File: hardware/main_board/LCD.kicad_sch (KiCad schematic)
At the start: 2 parts, among them J5 2x5 Socket Pins, U2 HiLetGo_ST7735R

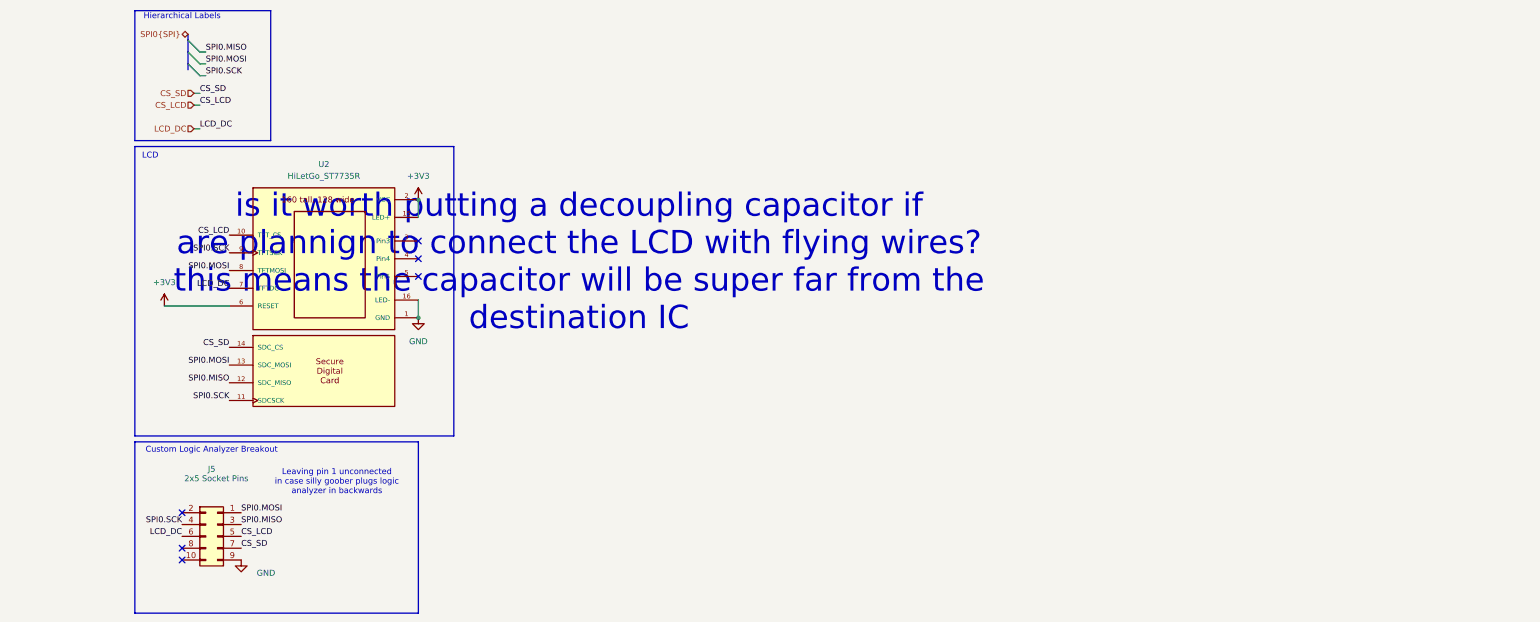
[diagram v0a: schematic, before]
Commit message: main board stuff. removed usbc for power. added level shifter for led logic signal. added lights for mux select signals. finished layout + pass DRC
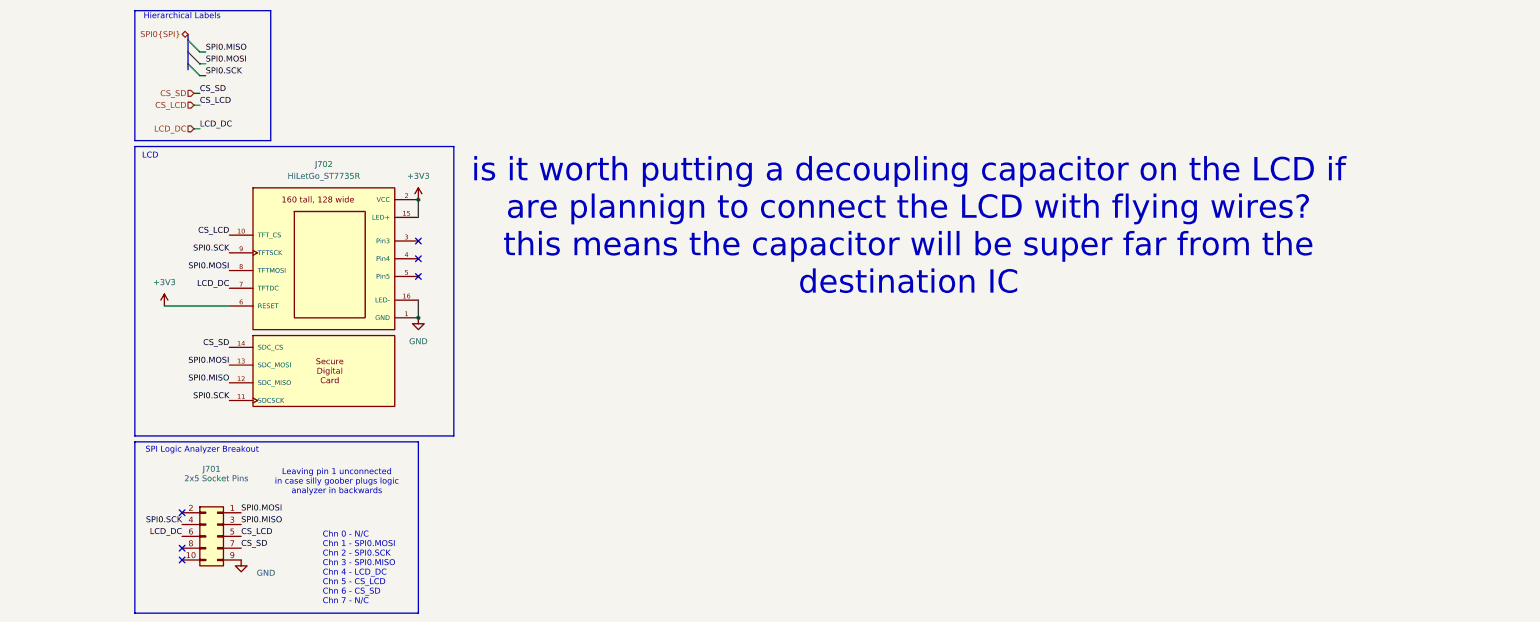
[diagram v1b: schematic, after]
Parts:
- renumbered J5 to J701, U2 to J702
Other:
- note added: "Chn 0 - N/C Chn 1 - SPI0.MOSI Chn 2 - SPI0.SCK Chn 3 - SPI0.MISO Chn 4 - LCD_DC Chn 5 - CS_LCD Chn 6 - CS_SD Chn 7 - N/C"
- note added: "SPI Logic Analyzer Breakout"
- note added: "is it worth putting a decoupling capacitor on the LCD if are plannign to connect the LCD with flying wires? this means the capacitor will be super far from the destination IC"
- note removed: "Custom Logic Analyzer Breakout"
- note removed: "is it worth putting a decoupling capacitor if are plannign to connect the LCD with flying wires? this means the capacitor will be super far from the destination IC"
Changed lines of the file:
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@@
 		)
 	)
-	(text "Custom Logic Analyzer Breakout"
-		(exclude_from_sim no)
-		(at 31.75 108.458 0)
+	(text "SPI Logic Analyzer Breakout"
+		(exclude_from_sim no)
+		(at 29.718 108.458 0)
 		(effects
 			(font
@@
 		)
 	)
-	(text "is it worth putting a decoupling capacitor if\nare plannign to connect the LCD with flying wires?\nthis means the capacitor will be super far from the \ndestination IC"
-		(exclude_from_sim no)
-		(at 110.744 68.072 0)
+	(text "Chn 0 - N/C\nChn 1 - SPI0.MOSI\nChn 2 - SPI0.SCK\nChn 3 - SPI0.MISO\nChn 4 - LCD_DC\nChn 5 - CS_LCD\nChn 6 - CS_SD\nChn 7 - N/C"
+		(exclude_from_sim no)
+		(at 55.626 133.858 0)
+		(effects
+			(font
+				(size 1.27 1.27)
+			)
+			(justify left)
+		)
+	)
+	(text "is it worth putting a decoupling capacitor on the LCD if\nare plannign to connect the LCD with flying wires?\nthis means the capacitor will be super far from the \ndestination IC"
+		(exclude_from_sim no)
+		(at 181.61 60.452 0)
 		(effects
 			(font
 				(size 5 5)
+				(color 255 0 59 1)
 			)
 		)
@@
 		(on_board yes)
 		(dnp no)
-		(property "Reference" "#PWR024"
+		(property "Reference" "#PWR0702"
 			(at 38.1 138.43 0)
 			(effects
@@
 			(project "main_board"
 				(path "/5332464e-0c3a-49d2-8fb5-731d0e42ee15/f60196d5-a61c-416f-993a-faa1a0858c5e"
-					(reference "#PWR024")
+					(reference "#PWR0702")
 					(unit 1)
 				)
@@
 		(dnp no)
 		(fields_autoplaced yes)
-		(property "Reference" "#PWR022"
+		(property "Reference" "#PWR0701"
 			(at 21.59 81.28 0)
 			(effects
@@
 			(project ""
 				(path "/5332464e-0c3a-49d2-8fb5-731d0e42ee15/f60196d5-a61c-416f-993a-faa1a0858c5e"
-					(reference "#PWR022")
+					(reference "#PWR0701")
 					(unit 1)
 				)
@@
 		(dnp no)
 		(fields_autoplaced yes)
-		(property "Reference" "#PWR021"
+		(property "Reference" "#PWR0703"
 			(at 76.2 58.42 0)
 			(effects
@@
 			(project "main_board"
 				(path "/5332464e-0c3a-49d2-8fb5-731d0e42ee15/f60196d5-a61c-416f-993a-faa1a0858c5e"
-					(reference "#PWR021")
+					(reference "#PWR0703")
 					(unit 1)
 				)
@@
 		(on_board yes)
 		(dnp no)
-		(property "Reference" "J5"
+		(property "Reference" "J701"
 			(at 31.75 112.522 0)
 			(effects
@@
 			(project "main_board"
 				(path "/5332464e-0c3a-49d2-8fb5-731d0e42ee15/f60196d5-a61c-416f-993a-faa1a0858c5e"
-					(reference "J5")
+					(reference "J701")
 					(unit 1)
 				)
@@
 		(dnp no)
 		(fields_autoplaced yes)
-		(property "Reference" "U2"
+		(property "Reference" "J702"
 			(at 55.88 46.99 0)
 			(effects
@@
 			(project "main_board"
 				(path "/5332464e-0c3a-49d2-8fb5-731d0e42ee15/f60196d5-a61c-416f-993a-faa1a0858c5e"
-					(reference "U2")
+					(reference "J702")
 					(unit 1)
 				)
@@
 		(dnp no)
 		(fields_autoplaced yes)
-		(property "Reference" "#PWR023"
+		(property "Reference" "#PWR0704"
 			(at 76.2 86.36 0)
 			(effects
@@
 			(project ""
 				(path "/5332464e-0c3a-49d2-8fb5-731d0e42ee15/f60196d5-a61c-416f-993a-faa1a0858c5e"
-					(reference "#PWR023")
+					(reference "#PWR0704")
 					(unit 1)
 				)

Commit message: bom
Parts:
- J701: now left out of the parts list
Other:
- note added: "50 mA"
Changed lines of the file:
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@@
+		)
+	)
+	(text "50 mA"
+		(exclude_from_sim no)
+		(at 18.542 104.394 0)
+		(effects
+			(font
+				(size 1.27 1.27)
+			)
 		)
 	)
@@
 		(unit 1)
 		(exclude_from_sim no)
-		(in_bom yes)
+		(in_bom no)
 		(on_board yes)
 		(dnp no)
